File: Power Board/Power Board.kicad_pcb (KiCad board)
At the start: 2 copper layers, 80 x 45.7 mm, 60 parts, among them J1 Conn_02x15_Counter_Clockwise, Q1 SI7135DP, Q2 SI7135DP, Q3 SI7135DP, Q4 SI7135DP, Q5 SI7135DP, Q6 SI7135DP, U1 LTC4417CGN, U2 TPS54308DDC, U3 TPS54308DDC, U4 TPS54308DDC

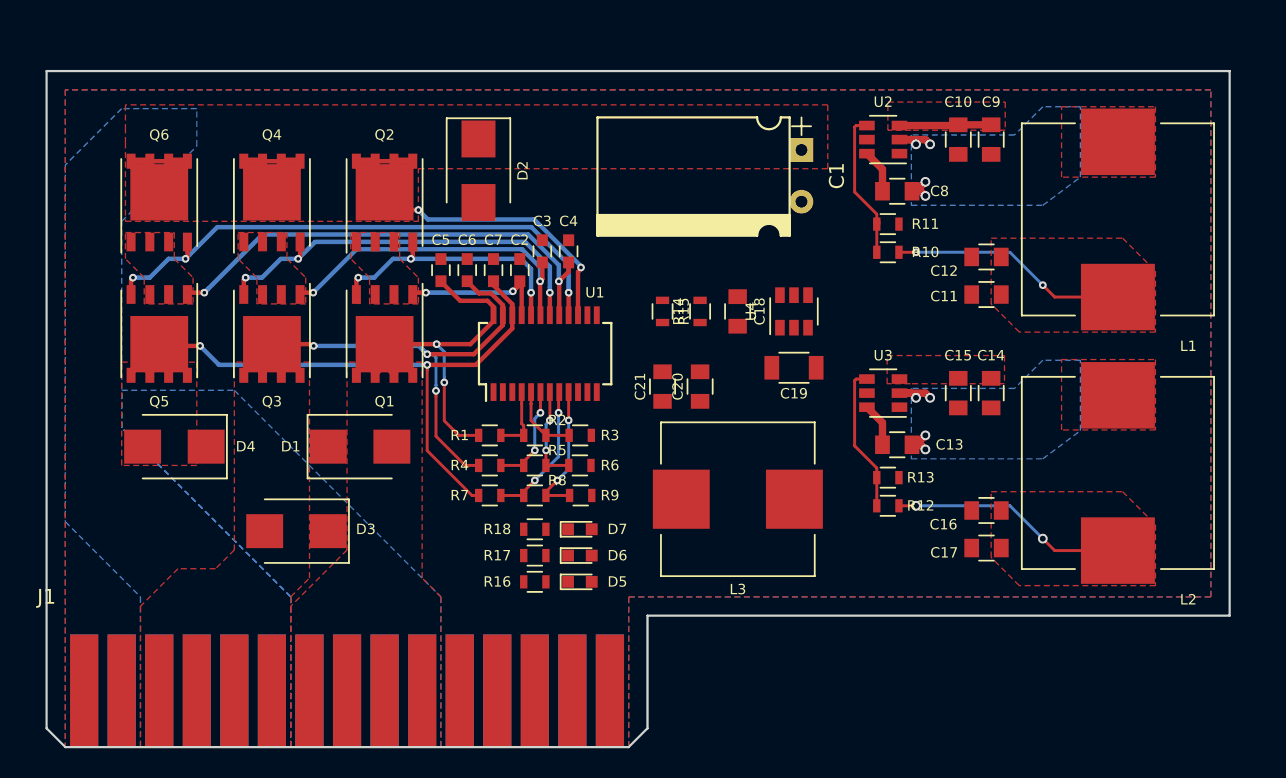
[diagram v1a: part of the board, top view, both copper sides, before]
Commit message: Finished routing power board
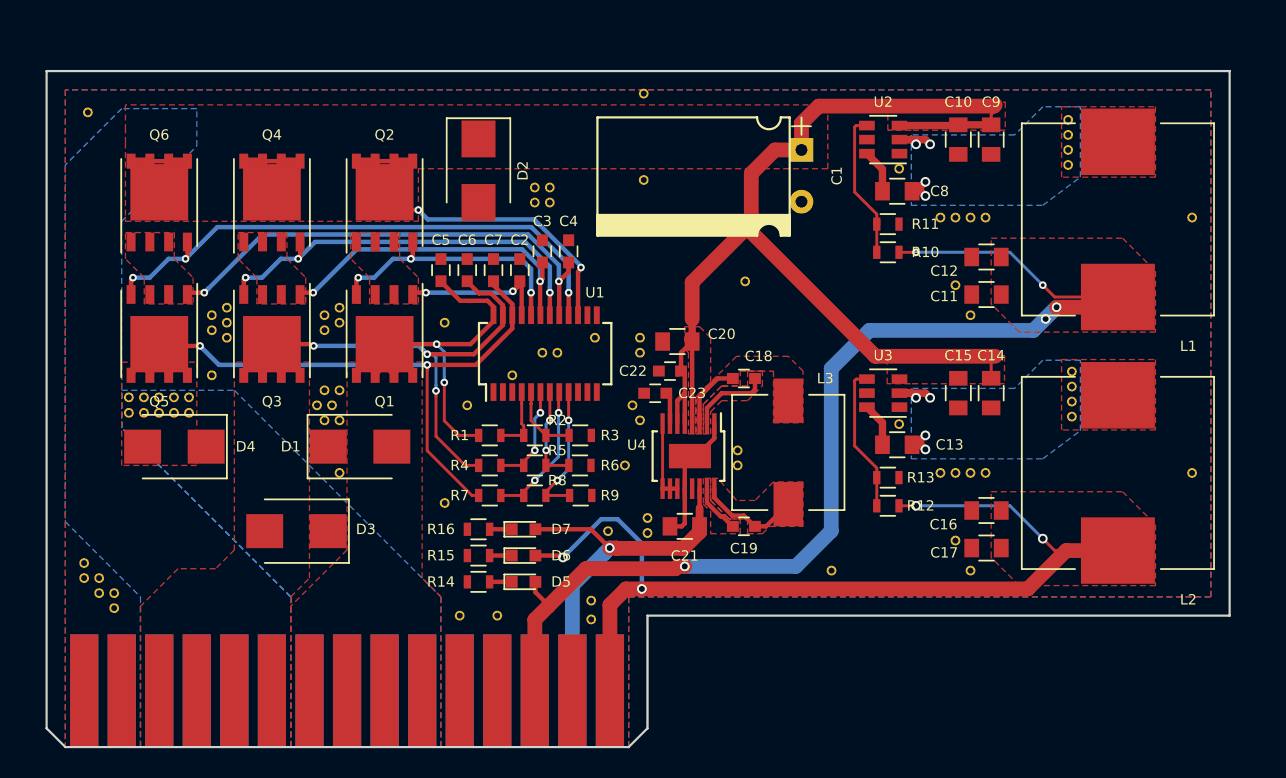
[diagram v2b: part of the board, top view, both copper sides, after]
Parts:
- removed the C21 at (95.0, 114.0)
- removed the R14 at (97.5, 109.0)
- removed the R15 at (95.0, 109.0)
- added C20: 15 uF, Capacitors_SMD:C_0805, F.Cu at (96.0, 111.0)
- added C22: 1 uF, Capacitors_SMD:C_0603, F.Cu at (95.5, 113.0)
- added C23: 4.7 uF, Capacitors_SMD:C_0603, F.Cu at (94.5, 114.5)
- added REF**: VIA_0.66mm, Custom Footprints:VIA_0.66mm, F.Cu at (91.3, 123.8)
- added REF**: VIA_0.66mm, Custom Footprints:VIA_0.66mm, F.Cu at (60.9, 115.8)
- added REF**: VIA_0.66mm, Custom Footprints:VIA_0.66mm, F.Cu at (60.9, 114.8)
- added REF**: VIA_0.66mm, Custom Footprints:VIA_0.66mm, F.Cu at (59.9, 115.8)
- added REF**: VIA_0.66mm, Custom Footprints:VIA_0.66mm, F.Cu at (59.9, 114.8)
- added REF**: VIA_0.66mm, Custom Footprints:VIA_0.66mm, F.Cu at (58.9, 115.8)
- added REF**: VIA_0.66mm, Custom Footprints:VIA_0.66mm, F.Cu at (122.7, 116.1)
- added REF**: VIA_0.66mm, Custom Footprints:VIA_0.66mm, F.Cu at (122.7, 115.1)
- added REF**: VIA_0.66mm, Custom Footprints:VIA_0.66mm, F.Cu at (122.7, 114.0)
- added REF**: VIA_0.66mm, Custom Footprints:VIA_0.66mm, F.Cu at (122.7, 113.0)
- added REF**: VIA_0.66mm, Custom Footprints:VIA_0.66mm, F.Cu at (122.4, 99.1)
- added REF**: VIA_0.66mm, Custom Footprints:VIA_0.66mm, F.Cu at (81.3, 129.5)
- added REF**: VIA_0.66mm, Custom Footprints:VIA_0.66mm, F.Cu at (122.4, 98.0)
- added REF**: VIA_0.66mm, Custom Footprints:VIA_0.66mm, F.Cu at (122.4, 97.0)
- added REF**: VIA_0.66mm, Custom Footprints:VIA_0.66mm, F.Cu at (130.8, 102.6)
- added REF**: VIA_0.66mm, Custom Footprints:VIA_0.66mm, F.Cu at (130.8, 119.9)
- added REF**: VIA_0.66mm, Custom Footprints:VIA_0.66mm, F.Cu at (106.4, 126.5)
- added REF**: VIA_0.66mm, Custom Footprints:VIA_0.66mm, F.Cu at (100.6, 106.9)
- added REF**: VIA_0.66mm, Custom Footprints:VIA_0.66mm, F.Cu at (93.7, 100.1)
- added REF**: VIA_0.66mm, Custom Footprints:VIA_0.66mm, F.Cu at (93.7, 94.2)
- added REF**: VIA_0.66mm, Custom Footprints:VIA_0.66mm, F.Cu at (56.1, 95.5)
- added REF**: VIA_0.66mm, Custom Footprints:VIA_0.66mm, F.Cu at (111.0, 99.3)
- added REF**: VIA_0.66mm, Custom Footprints:VIA_0.66mm, F.Cu at (83.8, 129.5)
- added REF**: VIA_0.66mm, Custom Footprints:VIA_0.66mm, F.Cu at (111.0, 116.6)
- added REF**: VIA_0.66mm, Custom Footprints:VIA_0.66mm, F.Cu at (115.8, 109.2)
- added REF**: VIA_0.66mm, Custom Footprints:VIA_0.66mm, F.Cu at (114.8, 107.2)
- added REF**: VIA_0.66mm, Custom Footprints:VIA_0.66mm, F.Cu at (115.8, 126.5)
- added REF**: VIA_0.66mm, Custom Footprints:VIA_0.66mm, F.Cu at (114.8, 124.5)
- added REF**: VIA_0.66mm, Custom Footprints:VIA_0.66mm, F.Cu at (81.8, 115.3)
- added REF**: VIA_0.66mm, Custom Footprints:VIA_0.66mm, F.Cu at (80.3, 121.9)
- added REF**: VIA_0.66mm, Custom Footprints:VIA_0.66mm, F.Cu at (73.2, 114.3)
- added REF**: VIA_0.66mm, Custom Footprints:VIA_0.66mm, F.Cu at (72.1, 114.3)
- added REF**: VIA_0.66mm, Custom Footprints:VIA_0.66mm, F.Cu at (72.6, 115.3)
- added REF**: VIA_0.66mm, Custom Footprints:VIA_0.66mm, F.Cu at (90.2, 129.8)
- added REF**: VIA_0.66mm, Custom Footprints:VIA_0.66mm, F.Cu at (71.6, 115.3)
- added REF**: VIA_0.66mm, Custom Footprints:VIA_0.66mm, F.Cu at (72.1, 116.3)
- added REF**: VIA_0.66mm, Custom Footprints:VIA_0.66mm, F.Cu at (73.2, 116.3)
- added REF**: VIA_0.66mm, Custom Footprints:VIA_0.66mm, F.Cu at (73.2, 119.9)
- added REF**: VIA_0.66mm, Custom Footprints:VIA_0.66mm, F.Cu at (64.5, 113.3)
- added REF**: VIA_0.66mm, Custom Footprints:VIA_0.66mm, F.Cu at (94.0, 124.0)
- added REF**: VIA_0.66mm, Custom Footprints:VIA_0.66mm, F.Cu at (94.0, 122.9)
- added REF**: VIA_0.66mm, Custom Footprints:VIA_0.66mm, F.Cu at (100.1, 119.4)
- added REF**: VIA_0.66mm, Custom Footprints:VIA_0.66mm, F.Cu at (100.1, 118.4)
- added REF**: VIA_0.66mm, Custom Footprints:VIA_0.66mm, F.Cu at (93.5, 116.3)
- added REF**: VIA_0.66mm, Custom Footprints:VIA_0.66mm, F.Cu at (90.2, 128.5)
- added REF**: VIA_0.66mm, Custom Footprints:VIA_0.66mm, F.Cu at (93.5, 110.7)
- added REF**: VIA_0.66mm, Custom Footprints:VIA_0.66mm, F.Cu at (93.0, 115.3)
- added REF**: VIA_0.66mm, Custom Footprints:VIA_0.66mm, F.Cu at (93.5, 111.8)
- added REF**: VIA_0.66mm, Custom Footprints:VIA_0.66mm, F.Cu at (92.5, 119.4)
- added REF**: VIA_0.66mm, Custom Footprints:VIA_0.66mm, F.Cu at (84.8, 113.3)
- added REF**: VIA_0.66mm, Custom Footprints:VIA_0.66mm, F.Cu at (90.4, 110.7)
- added REF**: VIA_0.66mm, Custom Footprints:VIA_0.66mm, F.Cu at (86.9, 111.8)
- added REF**: VIA_0.66mm, Custom Footprints:VIA_0.66mm, F.Cu at (87.9, 111.8)
- added REF**: VIA_0.66mm, Custom Footprints:VIA_0.66mm, F.Cu at (87.4, 100.6)
- added REF**: VIA_0.66mm, Custom Footprints:VIA_0.66mm, F.Cu at (86.4, 100.6)
- added REF**: VIA_0.66mm, Custom Footprints:VIA_0.66mm, F.Cu at (63.0, 115.8)
- added REF**: VIA_0.66mm, Custom Footprints:VIA_0.66mm, F.Cu at (87.4, 101.6)
- added REF**: VIA_0.66mm, Custom Footprints:VIA_0.66mm, F.Cu at (86.4, 101.6)
- added REF**: VIA_0.66mm, Custom Footprints:VIA_0.66mm, F.Cu at (113.8, 102.6)
- added REF**: VIA_0.66mm, Custom Footprints:VIA_0.66mm, F.Cu at (114.8, 102.6)
- added REF**: VIA_0.66mm, Custom Footprints:VIA_0.66mm, F.Cu at (115.8, 102.6)
- added REF**: VIA_0.66mm, Custom Footprints:VIA_0.66mm, F.Cu at (116.8, 102.6)
- added REF**: VIA_0.66mm, Custom Footprints:VIA_0.66mm, F.Cu at (116.8, 119.9)
- added REF**: VIA_0.66mm, Custom Footprints:VIA_0.66mm, F.Cu at (115.8, 119.9)
- added REF**: VIA_0.66mm, Custom Footprints:VIA_0.66mm, F.Cu at (114.8, 119.9)
- added REF**: VIA_0.66mm, Custom Footprints:VIA_0.66mm, F.Cu at (113.8, 119.9)
- added REF**: VIA_0.66mm, Custom Footprints:VIA_0.66mm, F.Cu at (63.0, 114.8)
- added REF**: VIA_0.66mm, Custom Footprints:VIA_0.66mm, F.Cu at (80.3, 109.7)
- added REF**: VIA_0.66mm, Custom Footprints:VIA_0.66mm, F.Cu at (73.2, 108.7)
- added REF**: VIA_0.66mm, Custom Footprints:VIA_0.66mm, F.Cu at (73.2, 109.7)
- added REF**: VIA_0.66mm, Custom Footprints:VIA_0.66mm, F.Cu at (72.1, 109.2)
- added REF**: VIA_0.66mm, Custom Footprints:VIA_0.66mm, F.Cu at (72.1, 110.2)
- added REF**: VIA_0.66mm, Custom Footprints:VIA_0.66mm, F.Cu at (65.5, 108.7)
- added REF**: VIA_0.66mm, Custom Footprints:VIA_0.66mm, F.Cu at (64.5, 109.2)
- added REF**: VIA_0.66mm, Custom Footprints:VIA_0.66mm, F.Cu at (65.5, 109.7)
- added REF**: VIA_0.66mm, Custom Footprints:VIA_0.66mm, F.Cu at (64.5, 110.2)
- added REF**: VIA_0.66mm, Custom Footprints:VIA_0.66mm, F.Cu at (65.5, 110.7)
- added REF**: VIA_0.66mm, Custom Footprints:VIA_0.66mm, F.Cu at (62.0, 115.8)
- added REF**: VIA_0.66mm, Custom Footprints:VIA_0.66mm, F.Cu at (57.9, 129.0)
- added REF**: VIA_0.66mm, Custom Footprints:VIA_0.66mm, F.Cu at (57.9, 128.0)
- added REF**: VIA_0.66mm, Custom Footprints:VIA_0.66mm, F.Cu at (56.9, 128.0)
- added REF**: VIA_0.66mm, Custom Footprints:VIA_0.66mm, F.Cu at (56.9, 127.0)
- added REF**: VIA_0.66mm, Custom Footprints:VIA_0.66mm, F.Cu at (55.9, 127.0)
- added REF**: VIA_0.66mm, Custom Footprints:VIA_0.66mm, F.Cu at (55.9, 126.0)
- added REF**: VIA_0.66mm, Custom Footprints:VIA_0.66mm, F.Cu at (122.4, 96.0)
- added REF**: VIA_0.66mm, Custom Footprints:VIA_0.66mm, F.Cu at (58.9, 114.8)
- added REF**: VIA_0.66mm, Custom Footprints:VIA_0.66mm, F.Cu at (62.0, 114.8)
- C18: value 0.1 uF -> 22nF; footprint Capacitors_SMD:C_0805 -> Capacitors_SMD:C_0603
- C19: value 33 uF -> 22nF; footprint Capacitors_SMD:C_1206 -> Capacitors_SMD:C_0603
- L3: value 16 uH -> 15 uH; footprint Inductors_SMD:L_Wuerth_HCI-1050 -> Custom Footprints:L_Wuerth_7447779115
- R1: value 93.1 kΩ -> 90.9 kΩ
- R2: value 309 Ω -> 4.99 kΩ
- R3: value 5.36 kΩ -> 4.99 kΩ
- R4, R7: value 93.1 kΩ -> 82.5 kΩ
- R5, R8: value 2.49 kΩ -> 5.49 kΩ
- R6, R9: value 5.9 kΩ -> 11 kΩ
- U4: value TPS54308DDC -> LTC3130-1; footprint TO_SOT_Packages_SMD:SOT-23-6 -> Housings_SSOP:MSOP-16-1EP_3x4mm_Pitch0.5mm
- moved U4 12.1 mm to (96.8, 118.8), turned to 270 degrees
- moved C19 11.2 mm to (100.5, 123.5)
- moved C21 9.51 mm to (96.5, 123.5), turned to 180 degrees
- moved L3 4.65 mm to (103.5, 118.5), turned to 270 degrees
- moved C18 4.55 mm to (100.5, 113.5), turned to 180 degrees
- moved D5 3.81 mm to (85.6, 127.3)
- moved D6 3.81 mm to (85.6, 125.5)
- moved D7 3.81 mm to (85.6, 123.7)
- moved R14 3.81 mm to (82.5, 127.3)
- moved R15 3.81 mm to (82.5, 125.5)
- moved R16 3.81 mm to (82.5, 123.7)
- renumbered C20 to C21, R16 to R14, R17 to R15, R18 to R16
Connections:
- C19 pad 1: +14V -> Net-(C19-Pad1)
- C19 pad 2: GND -> Net-(C19-Pad2)
- L3 pad 2: +12V -> Net-(C19-Pad1)
- U4 pad 2: Net-(C18-Pad2) -> Net-(C18-Pad1)
- U4 pad 3: +14V -> Net-(C18-Pad2)
- U4 pad 4: Net-(R14-Pad2) -> +14V
- U4 pad 5: (no net) -> +14V
- U4 pad 6: Net-(C18-Pad1) -> +14V
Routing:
- net +14V: track 36.4 -> 112.1 mm
- net +3V3: track 16.2 -> 77.9 mm, vias 2 -> 5
- net /XBEE_VCC: track 16.3 -> 70.1 mm, vias 2 -> 4
- net +12V: track 0.00 -> 26.9 mm, vias 0 -> 1
- net GND: track 0.00 -> 8.92 mm
- net Net-(C19-Pad1): track 0.00 -> 7.04 mm
- net Net-(C18-Pad1): track 0.00 -> 5.57 mm
- net Net-(C18-Pad2): track 0.00 -> 4.58 mm
- net Net-(C19-Pad2): track 0.00 -> 3.36 mm
- net Net-(C23-Pad1): track 0.00 -> 2.15 mm
- net Net-(D7-Pad1): track 0.00 -> 1.50 mm
- net Net-(D6-Pad1): track 0.00 -> 1.50 mm
- net Net-(D5-Pad1): track 0.00 -> 1.50 mm
- added copper zone on F.Cu, net Net-(C18-Pad1)
- added copper zone on F.Cu, net Net-(C18-Pad2)
- added copper zone on F.Cu, net Net-(C19-Pad1)
- added copper zone on F.Cu, net Net-(C19-Pad2)

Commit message: Fixed a few little things
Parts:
- added REF**: VIA_0.52mm, Custom Footprints:VIA_0.52mm, F.Cu at (98.0, 119.2)
- added REF**: VIA_0.52mm, Custom Footprints:VIA_0.52mm, F.Cu at (98.0, 118.2)
- added REF**: VIA_0.52mm, Custom Footprints:VIA_0.52mm, F.Cu at (97.5, 118.8)
- added REF**: VIA_0.52mm, Custom Footprints:VIA_0.52mm, F.Cu at (96.8, 119.2)
- added REF**: VIA_0.52mm, Custom Footprints:VIA_0.52mm, F.Cu at (97.0, 118.2)
- added REF**: VIA_0.52mm, Custom Footprints:VIA_0.52mm, F.Cu at (96.2, 118.8)
- added REF**: VIA_0.52mm, Custom Footprints:VIA_0.52mm, F.Cu at (95.8, 119.2)
- added REF**: VIA_0.52mm, Custom Footprints:VIA_0.52mm, F.Cu at (95.8, 118.2)
- moved REF** 0.19 mm to (122.5, 116.1)
- moved REF** 0.19 mm to (122.5, 115.1)
- moved REF** 0.19 mm to (122.5, 114.0)
- moved REF** 0.19 mm to (122.5, 113.0)
- moved REF** 0.06 mm to (122.5, 99.1)
- moved REF** 0.06 mm to (122.5, 98.0)
- moved REF** 0.06 mm to (122.5, 97.0)
- moved REF** 0.06 mm to (122.5, 96.0)
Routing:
- net +3V3: track 77.9 -> 79.0 mm

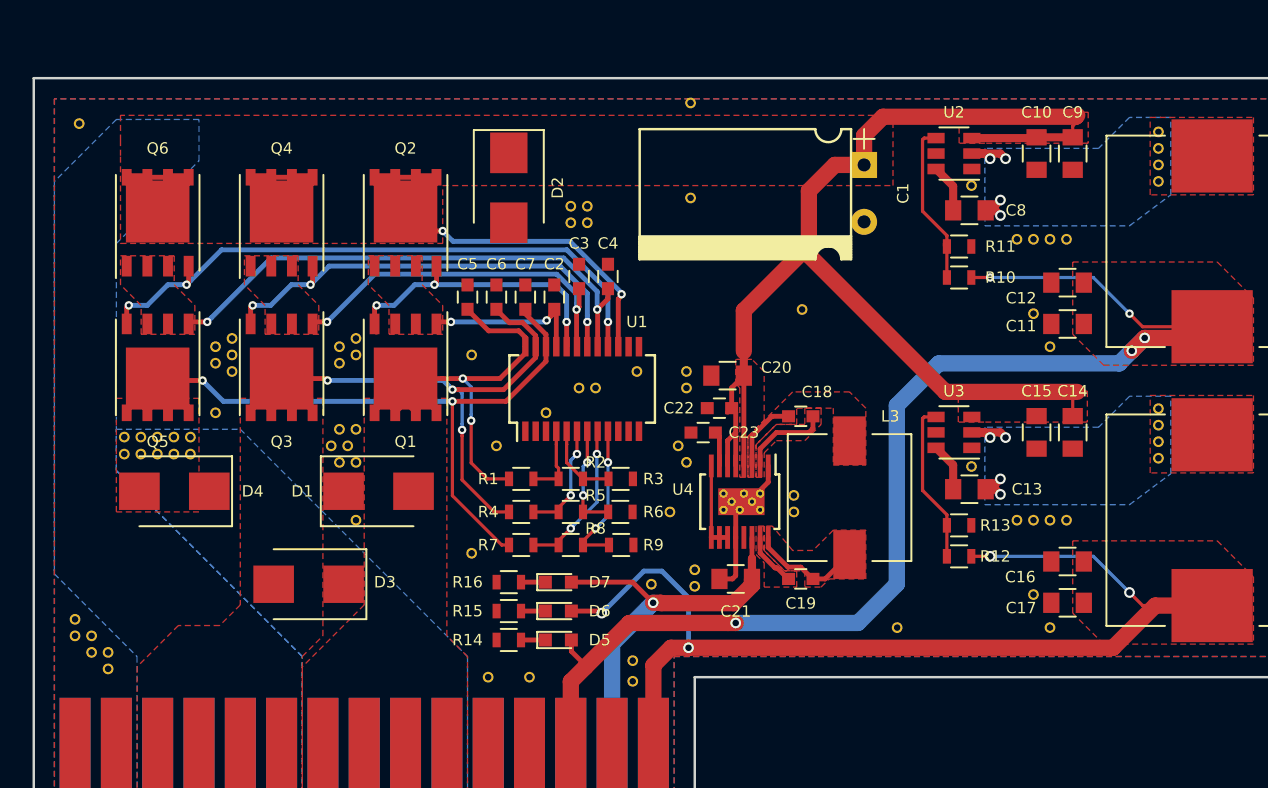
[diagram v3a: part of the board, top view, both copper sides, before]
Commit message: Ready for power PCB review
Also added a kick-ass logo to the backside
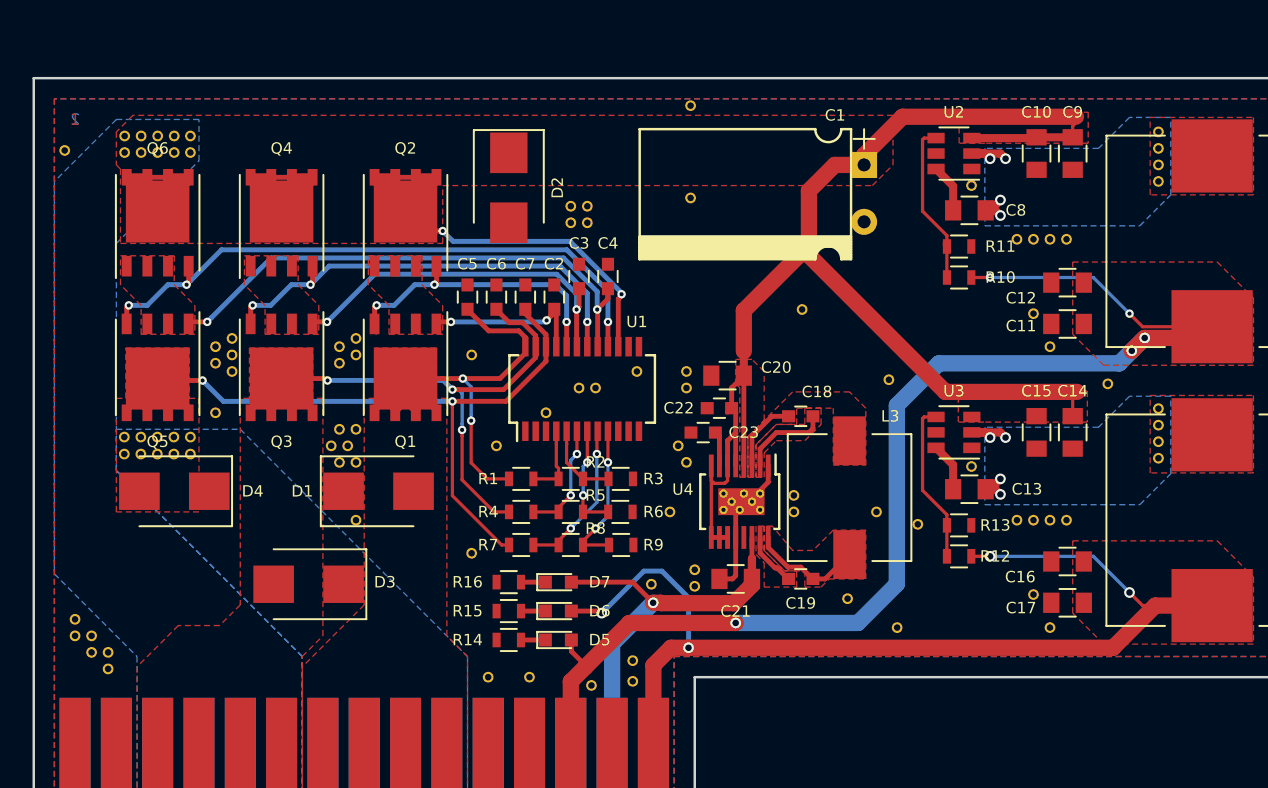
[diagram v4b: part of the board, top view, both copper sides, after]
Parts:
- added G***: LOGO, Custom Parts:Logo_v2, B.Cu at (123.2, 111.8)
- added REF**: VIA_0.66mm, Custom Footprints:VIA_0.66mm, F.Cu at (103.4, 124.7)
- added REF**: VIA_0.66mm, Custom Footprints:VIA_0.66mm, F.Cu at (62.0, 97.3)
- added REF**: VIA_0.66mm, Custom Footprints:VIA_0.66mm, F.Cu at (62.0, 96.3)
- added REF**: VIA_0.66mm, Custom Footprints:VIA_0.66mm, F.Cu at (63.0, 96.3)
- added REF**: VIA_0.66mm, Custom Footprints:VIA_0.66mm, F.Cu at (63.0, 97.3)
- added REF**: VIA_0.66mm, Custom Footprints:VIA_0.66mm, F.Cu at (105.9, 111.3)
- added REF**: VIA_0.66mm, Custom Footprints:VIA_0.66mm, F.Cu at (105.2, 119.4)
- added REF**: VIA_0.66mm, Custom Footprints:VIA_0.66mm, F.Cu at (107.7, 120.1)
- added REF**: VIA_0.66mm, Custom Footprints:VIA_0.66mm, F.Cu at (119.4, 111.5)
- added REF**: VIA_0.66mm, Custom Footprints:VIA_0.66mm, F.Cu at (87.6, 130.0)
- added REF**: VIA_0.66mm, Custom Footprints:VIA_0.66mm, F.Cu at (58.9, 96.3)
- added REF**: VIA_0.66mm, Custom Footprints:VIA_0.66mm, F.Cu at (58.9, 97.3)
- added REF**: VIA_0.66mm, Custom Footprints:VIA_0.66mm, F.Cu at (59.9, 97.3)
- added REF**: VIA_0.66mm, Custom Footprints:VIA_0.66mm, F.Cu at (59.9, 96.3)
- added REF**: VIA_0.66mm, Custom Footprints:VIA_0.66mm, F.Cu at (61.0, 96.3)
- added REF**: VIA_0.66mm, Custom Footprints:VIA_0.66mm, F.Cu at (61.0, 97.3)
- moved REF** 1.88 mm to (55.2, 97.2)
- moved REF** 0.17 mm to (93.7, 94.4)
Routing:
- net /BAT_VCC: track 41.4 -> 30.9 mm
- net /BAT_BAK_VCC: track 50.3 -> 41.5 mm
- net +14V: track 112.1 -> 114.2 mm
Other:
- rule pad_to_mask_clearance: 0.00001 -> 0.05
- board text added: "1"
- board text added: "2"
- board text added: "Power Board v0.2 UAH SHC Spaceport America Cup 2018 Designed by Thomas Bennett"

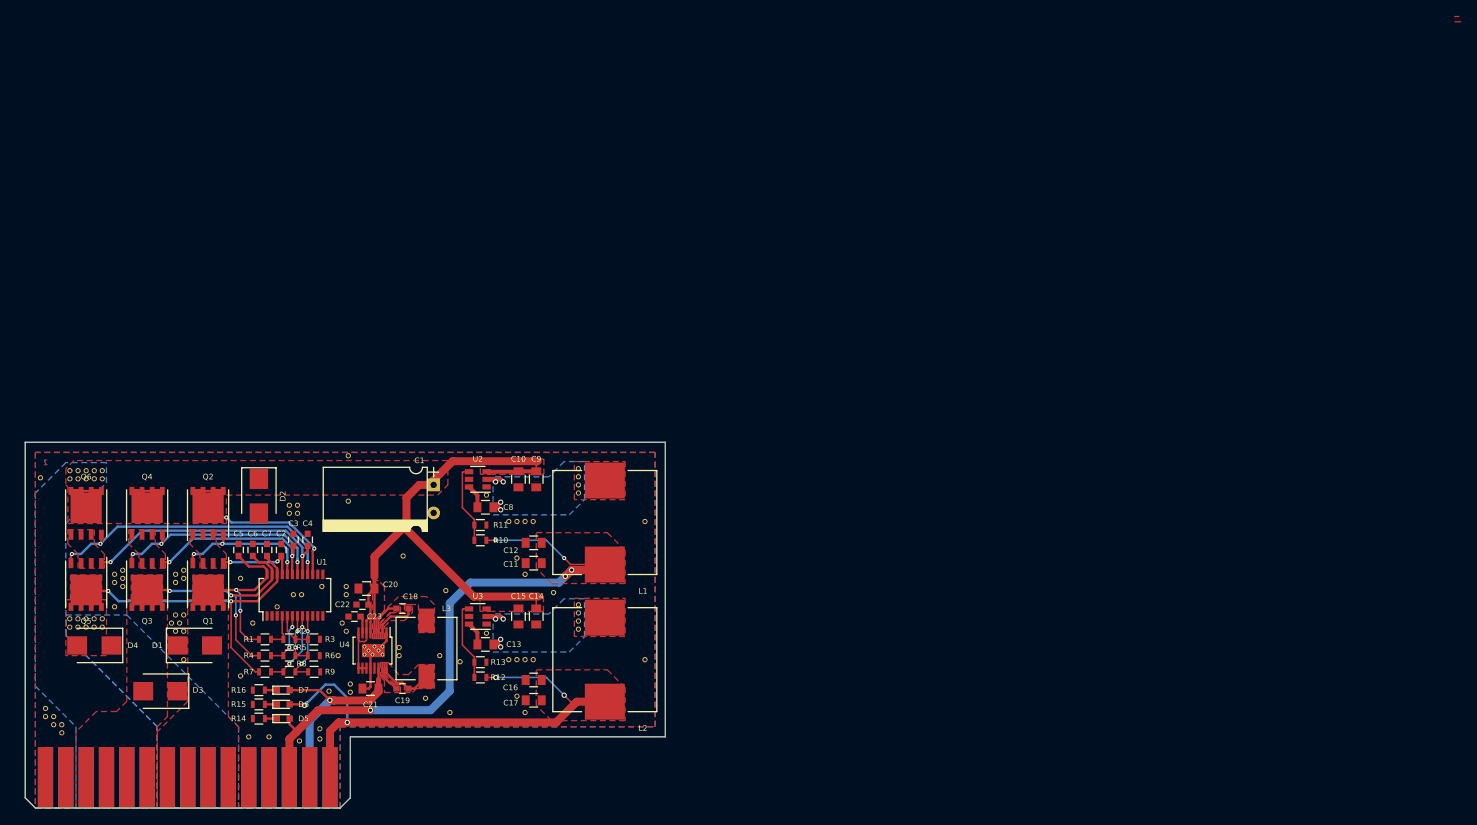
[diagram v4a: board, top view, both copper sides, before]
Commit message: Updated some clearances and sizes
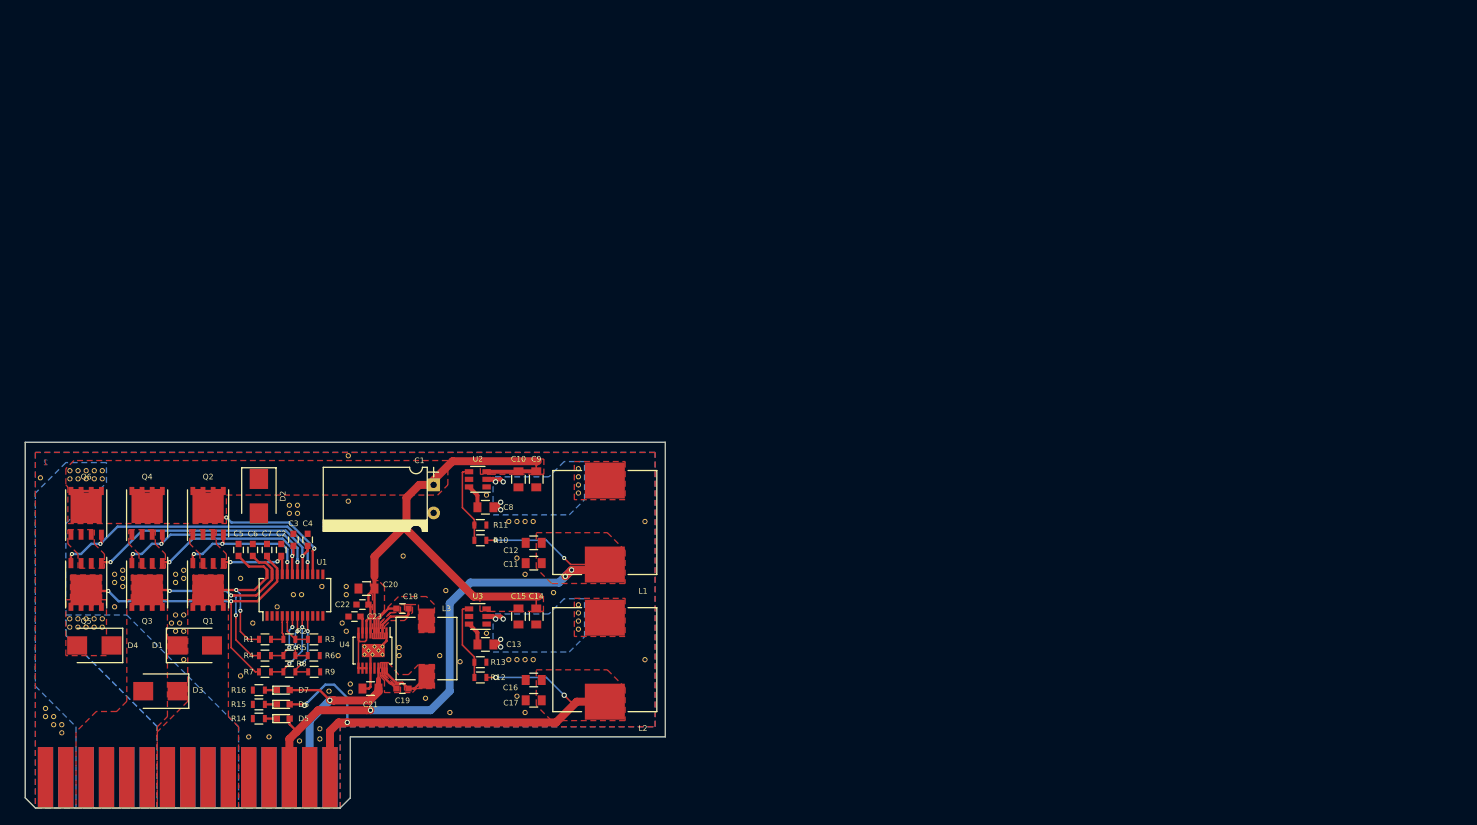
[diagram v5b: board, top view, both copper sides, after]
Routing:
- net (no net): track 1.25 -> 0.00 mm
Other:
- net class Small: clearance 0.13 -> 0.16; trace_width 0.13 -> 0.16; via_drill 0.25 -> 0.254
- rule pad_to_mask_clearance: 0.05 -> 0.0254
- rule solder_mask_min_width: 0.1 -> 0.1016
- rule trace_min: 0.13 -> 0.1524
- rule via_min_drill: 0.25 -> 0.254
- rule via_min_size: 0.51 -> 0.508
- board text added: "Power Board v0.3 UAH SHC Spaceport America Cup 2018 Designed by Thomas Bennett"
- board text removed: "Power Board v0.2 UAH SHC Spaceport America Cup 2018 Designed by Thomas Bennett"
